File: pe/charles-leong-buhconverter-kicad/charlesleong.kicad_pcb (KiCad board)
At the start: 2 copper layers, 1 part, among them U1 TPS542025DDCR

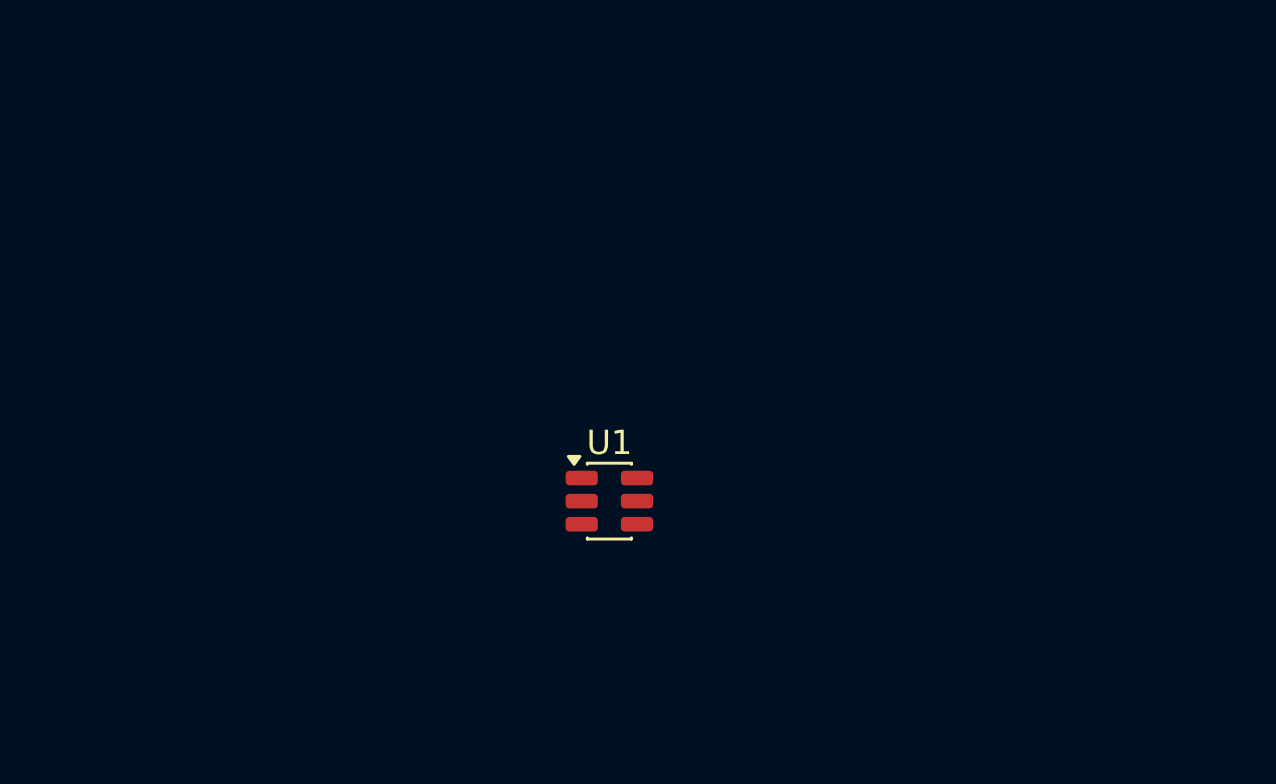
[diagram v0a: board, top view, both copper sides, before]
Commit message: added pcb footprints
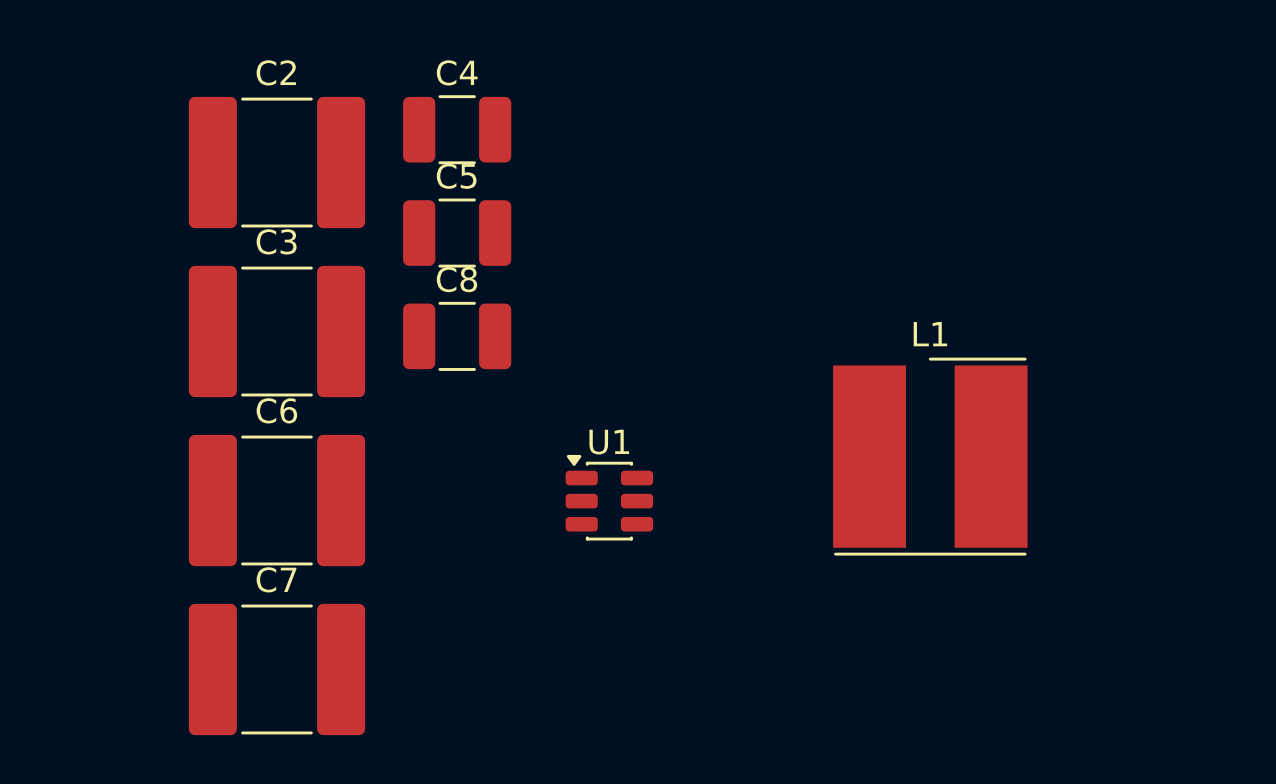
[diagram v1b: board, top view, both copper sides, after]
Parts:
- added C2: 10μf, Capacitor_SMD:C_2220_5750Metric_Pad1.97x5.40mm_HandSolder, F.Cu at (105.9, 62.0)
- added C3: 10μf, Capacitor_SMD:C_2220_5750Metric_Pad1.97x5.40mm_HandSolder, F.Cu at (105.9, 68.9)
- added C4: 100nF, Capacitor_SMD:C_1210_3225Metric_Pad1.33x2.70mm_HandSolder, F.Cu at (113.3, 60.6)
- added C5: 100nF, Capacitor_SMD:C_1210_3225Metric_Pad1.33x2.70mm_HandSolder, F.Cu at (113.3, 64.9)
- added C6: 10μf, Capacitor_SMD:C_2220_5750Metric_Pad1.97x5.40mm_HandSolder, F.Cu at (105.9, 75.9)
- added C7: 10μf, Capacitor_SMD:C_2220_5750Metric_Pad1.97x5.40mm_HandSolder, F.Cu at (105.9, 82.8)
- added C8: 100nF, Capacitor_SMD:C_1210_3225Metric_Pad1.33x2.70mm_HandSolder, F.Cu at (113.3, 69.1)
- added L1: 12 µH, formula_slug_footprint_library:L_Wurth_WE-PD2SR-7850, F.Cu at (132.8, 74.1)

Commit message: pcb components
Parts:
- moved C6 35.7 mm to (141.4, 79.0)
- moved C7 27.7 mm to (141.0, 70.5)
- moved C5 26.1 mm to (131.9, 79.0)
- moved C1 11.1 mm to (100.1, 71.5)
- moved C4 9.88 mm to (123.1, 66.5)
- moved L1 5.23 mm to (131.5, 69.0)
- moved C3 4.43 mm to (114.0, 65.0)
- moved C2 4.13 mm to (109.1, 71.5)
- moved U1 2.96 mm to (119.0, 73.0)
- renumbered C2 to C1, C3 to C2, C4 to C3, C5 to C4, C6 to C5, C7 to C6, C8 to C7
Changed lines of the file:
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@@
 		(capping no)
 		(filling no)
+		(zone_defaults)
 		(pcbplotparams
 			(layerselection 0x00000000_00000000_55555555_5755f5ff)
@@
 	(footprint "Capacitor_SMD:C_2220_5750Metric_Pad1.97x5.40mm_HandSolder"
 		(layer "F.Cu")
-		(at 105.905 82.825)
+		(at 141.3625 79)
 		(descr "Capacitor SMD 2220 (5750 Metric), square (rectangular) end terminal, IPC-7351 nominal with elongated pad for handsoldering. (Body size from: http://datasheets.avx.com/AVX-HV_MLCC.pdf)")
 		(tags "capacitor handsolder")
-		(property "Reference" "C7"
+		(property "Reference" "C6"
 			(at 0 -3.65 0)
 			(layer "F.SilkS")
@@
 	(footprint "Capacitor_SMD:C_1210_3225Metric_Pad1.33x2.70mm_HandSolder"
 		(layer "F.Cu")
-		(at 113.315 69.125)
+		(at 141 70.5)
 		(descr "Capacitor SMD 1210 (3225 Metric), square (rectangular) end terminal, IPC-7351 nominal with elongated pad for handsoldering. (Body size source: IPC-SM-782 page 76, https://www.pcb-3d.com/wordpress/wp-content/uploads/ipc-sm-782a_amendment_1_and_2.pdf)")
 		(tags "capacitor handsolder")
-		(property "Reference" "C8"
+		(property "Reference" "C7"
 			(at 0 -2.3 0)
 			(layer "F.SilkS")
@@
 	(footprint "Package_TO_SOT_SMD:SOT-23-6"
 		(layer "F.Cu")
-		(at 119.575 75.9)
+		(at 119 73)
 		(descr "SOT, 6 Pin (JEDEC MO-178 Var AB https://www.jedec.org/document_search?search_api_views_fulltext=MO-178)")
 		(tags "SOT TO_SOT_SMD")
@@
 	(footprint "Capacitor_SMD:C_1210_3225Metric_Pad1.33x2.70mm_HandSolder"
 		(layer "F.Cu")
-		(at 113.315 64.875)
+		(at 123.0625 66.5)
 		(descr "Capacitor SMD 1210 (3225 Metric), square (rectangular) end terminal, IPC-7351 nominal with elongated pad for handsoldering. (Body size source: IPC-SM-782 page 76, https://www.pcb-3d.com/wordpress/wp-content/uploads/ipc-sm-782a_amendment_1_and_2.pdf)")
 		(tags "capacitor handsolder")
-		(property "Reference" "C5"
+		(property "Reference" "C4"
 			(at 0 -2.3 0)
 			(layer "F.SilkS")
@@
 	(footprint "Capacitor_SMD:C_2220_5750Metric_Pad1.97x5.40mm_HandSolder"
 		(layer "F.Cu")
-		(at 105.905 75.875)
+		(at 131.8625 79)
 		(descr "Capacitor SMD 2220 (5750 Metric), square (rectangular) end terminal, IPC-7351 nominal with elongated pad for handsoldering. (Body size from: http://datasheets.avx.com/AVX-HV_MLCC.pdf)")
 		(tags "capacitor handsolder")
-		(property "Reference" "C6"
+		(property "Reference" "C5"
 			(at 0 -3.65 0)
 			(layer "F.SilkS")
@@
 	(footprint "formula_slug_footprint_library:L_Wurth_WE-PD2SR-7850"
 		(layer "F.Cu")
-		(at 132.775 74.07)
+		(at 131.5 69)
 		(descr "Shielded Power Inductor, body 7.8x7x5mm, https://www.we-online.com/en/components/products/WE-PD2SR#/articles/WE-PD2SR-7850")
 		(tags "SMT")
@@
 	(footprint "Capacitor_SMD:C_2220_5750Metric_Pad1.97x5.40mm_HandSolder"
 		(layer "F.Cu")
-		(at 105.905 68.925)
+		(at 109.1375 71.5)
 		(descr "Capacitor SMD 2220 (5750 Metric), square (rectangular) end terminal, IPC-7351 nominal with elongated pad for handsoldering. (Body size from: http://datasheets.avx.com/AVX-HV_MLCC.pdf)")
 		(tags "capacitor handsolder")
-		(property "Reference" "C3"
+		(property "Reference" "C2"
 			(at 0 -3.65 0)
 			(layer "F.SilkS")
@@
 	(footprint "Capacitor_SMD:C_2220_5750Metric_Pad1.97x5.40mm_HandSolder"
 		(layer "F.Cu")
-		(at 105.905 61.975)
+		(at 100.1375 71.5)
 		(descr "Capacitor SMD 2220 (5750 Metric), square (rectangular) end terminal, IPC-7351 nominal with elongated pad for handsoldering. (Body size from: http://datasheets.avx.com/AVX-HV_MLCC.pdf)")
 		(tags "capacitor handsolder")
-		(property "Reference" "C2"
+		(property "Reference" "C1"
 			(at 0 -3.65 0)
 			(layer "F.SilkS")
@@
 	(footprint "Capacitor_SMD:C_1210_3225Metric_Pad1.33x2.70mm_HandSolder"
 		(layer "F.Cu")
-		(at 113.315 60.625)
+		(at 114 65)
 		(descr "Capacitor SMD 1210 (3225 Metric), square (rectangular) end terminal, IPC-7351 nominal with elongated pad for handsoldering. (Body size source: IPC-SM-782 page 76, https://www.pcb-3d.com/wordpress/wp-content/uploads/ipc-sm-782a_amendment_1_and_2.pdf)")
 		(tags "capacitor handsolder")
-		(property "Reference" "C4"
+		(property "Reference" "C3"
 			(at 0 -2.3 0)
 			(layer "F.SilkS")

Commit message: aligning pcb components
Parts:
- moved C7 23.9 mm to (120.0, 82.0)
- moved L1 21.7 mm to (112.5, 79.5), turned to 90 degrees
- moved C6 17.3 mm to (126.0, 71.0), turned to 90 degrees
- moved C1 11.9 mm to (112.0, 72.0)
- moved C4 11.6 mm to (119.5, 77.5)
- moved C2 11.5 mm to (119.5, 66.5), turned to 90 degrees
- moved C5 5.88 mm to (126.0, 79.5), turned to -90 degrees
- moved C3 1.41 mm to (113.0, 66.0)
